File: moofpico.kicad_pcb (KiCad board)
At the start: 2 copper layers, 85.7 x 62.9 mm, 22 parts, among them J1 Conn_01x04, J100 Bus_Apple_II_Card_Side, J2 Micro_SD_Card_Det2, Q1 BS170, SW1 SW_DIP_x02, U2 74F11, U3 74LVC245, U4 74LVC245, U5 74LVC245, U6 RaspberryPi_Pico

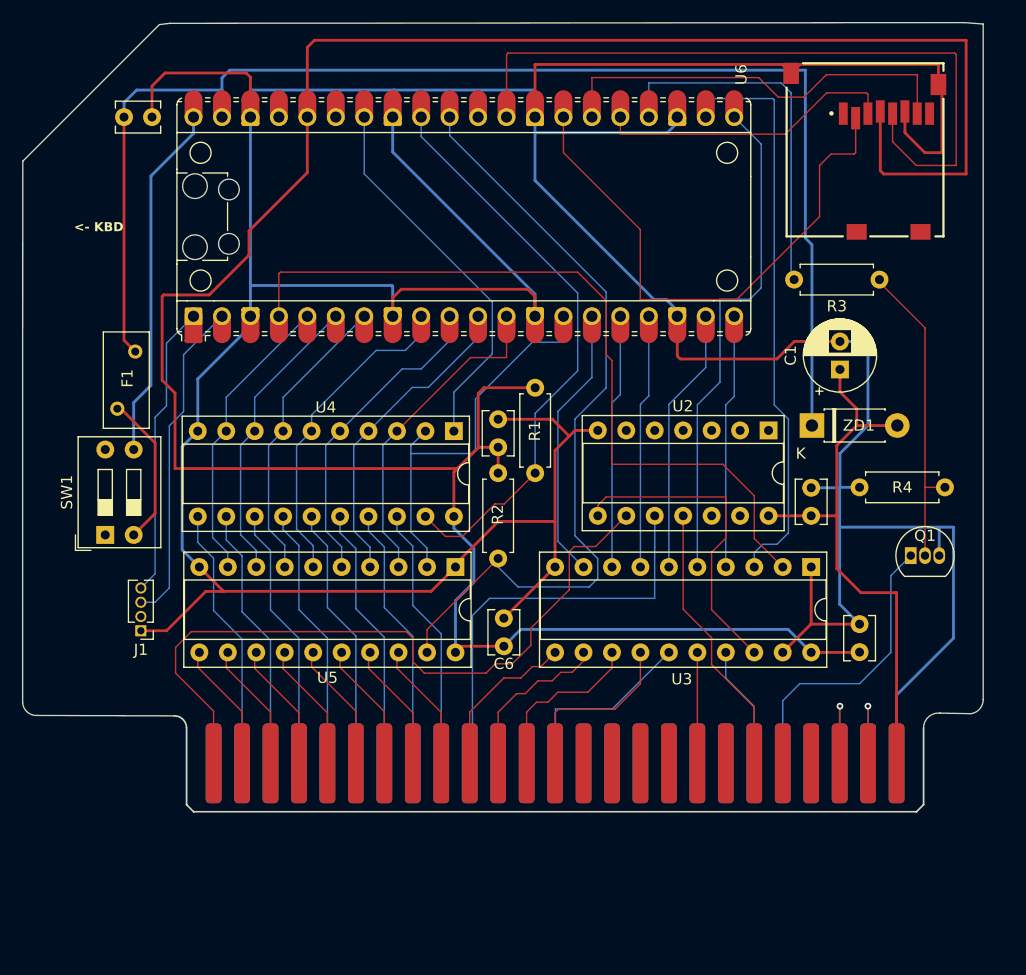
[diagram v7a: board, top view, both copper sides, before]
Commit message: swap nand pin assignments around
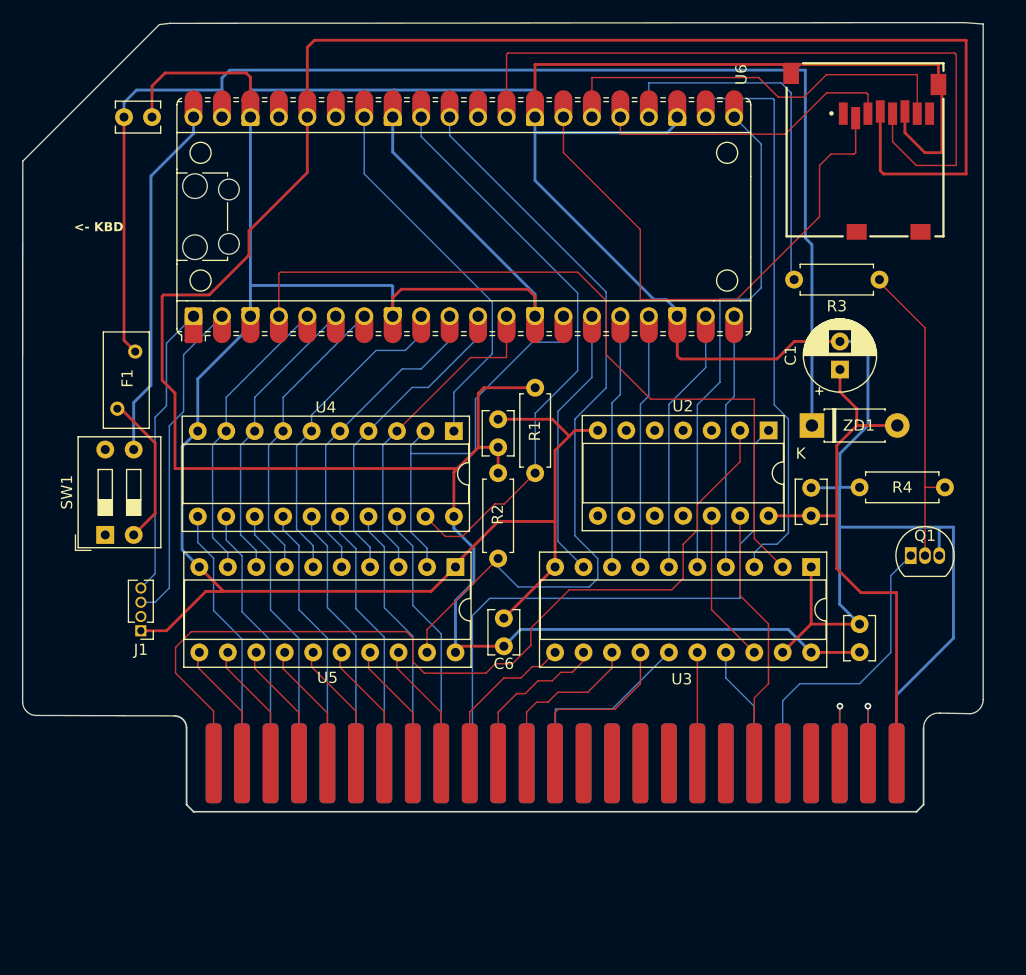
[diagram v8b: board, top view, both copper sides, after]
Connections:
- U2 pad 1: unconnected-(U2-Pad1) -> Net-(J100-~{DEVICE_SELECT})
- U2 pad 10: Net-(J100-~{DEVICE_SELECT}) -> unconnected-(U2-Pad10)
- U2 pad 11: Net-(J100-~{I/O_STROBE}) -> unconnected-(U2-Pad11)
- U2 pad 12: unconnected-(U2-Pad12) -> TTLENBL
- U2 pad 13: unconnected-(U2-Pad13) -> Net-(J100-~{I/O_STROBE})
- U2 pad 2: unconnected-(U2-Pad2) -> Net-(J100-~{I/O_SELECT})
- U2 pad 8: TTLENBL -> unconnected-(U2-Pad8)
- U2 pad 9: Net-(J100-~{I/O_SELECT}) -> unconnected-(U2-Pad9)
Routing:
- net Net-(J100-~{DEVICE_SELECT}): track 37.2 -> 53.5 mm
- net Net-(J100-~{I/O_SELECT}): track 64.0 -> 80.1 mm
- net TTLENBL: track 28.6 -> 13.8 mm
- net Net-(J100-~{I/O_STROBE}): track 24.7 -> 23.7 mm
